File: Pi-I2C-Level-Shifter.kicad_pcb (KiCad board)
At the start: 2 copper layers, 27.9 x 15.2 mm, 9 parts, among them J1 Conn_01x05, J4 Conn_01x05, U1 TXB0102DCT

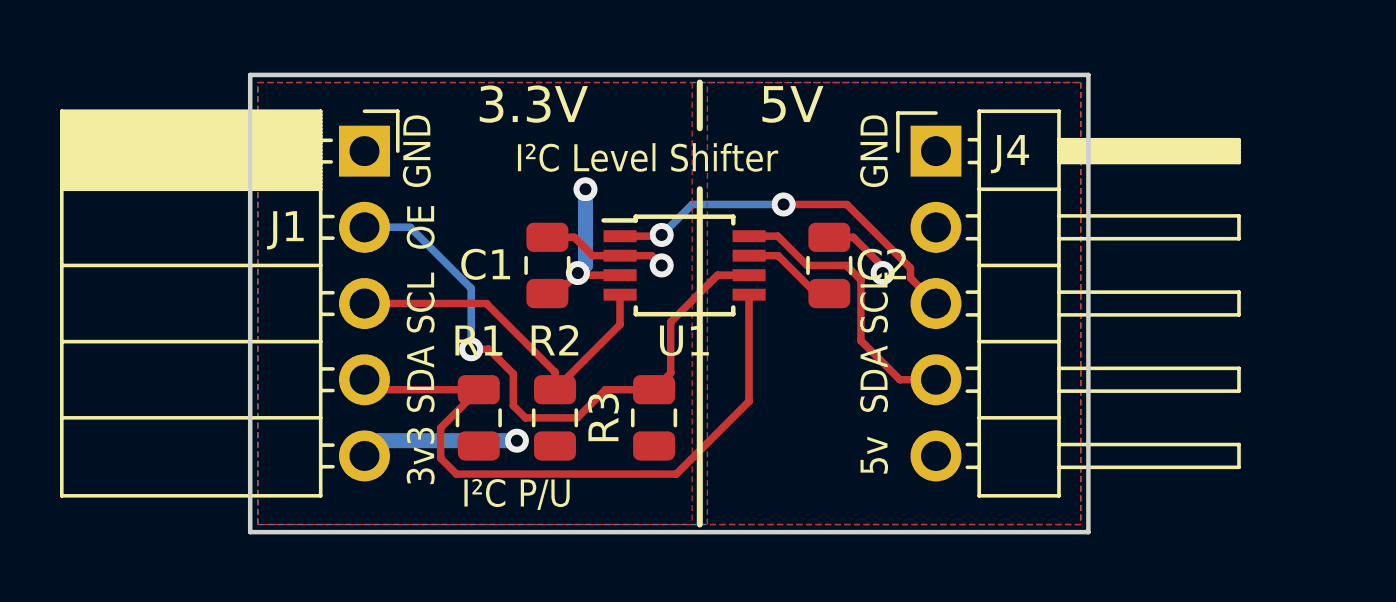
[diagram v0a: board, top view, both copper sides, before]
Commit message: Added 5v GPIO (8 bits)
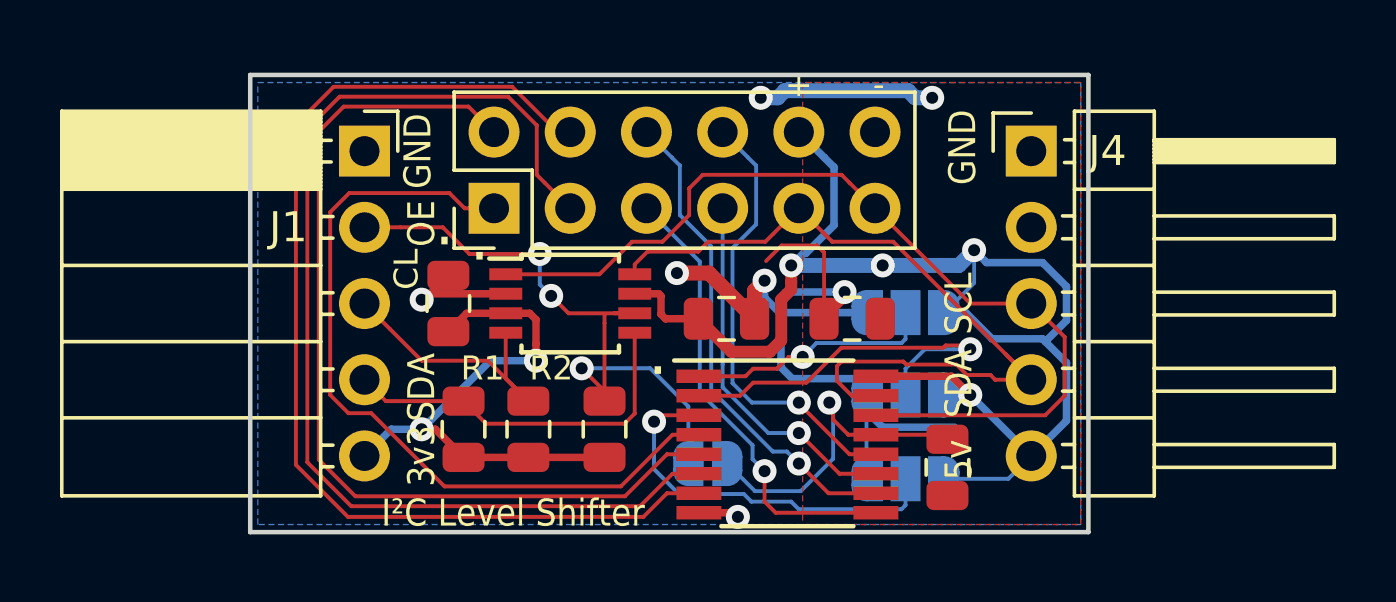
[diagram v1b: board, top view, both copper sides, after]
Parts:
- added C3: 0.1uF, Capacitor_SMD:C_0805_2012Metric, F.Cu at (199.1, 86.9)
- added J2: Conn_02x06_Odd_Even, Connector_PinHeader_2.54mm:PinHeader_2x06_P2.54mm_Vertical, F.Cu at (187.2, 83.2)
- added JP1: SolderJumper_2_Open, Jumper:SolderJumper-2_P1.3mm_Open_RoundedPad1.0x1.5mm, B.Cu at (194.3, 91.7)
- added JP2: SolderJumper_3_Open, Jumper:SolderJumper-3_P1.3mm_Open_RoundedPad1.0x1.5mm, B.Cu at (200.9, 92.2)
- added JP3: SolderJumper_3_Open, Jumper:SolderJumper-3_P1.3mm_Open_RoundedPad1.0x1.5mm, B.Cu at (200.9, 89.4)
- added JP4: SolderJumper_3_Open, Jumper:SolderJumper-3_P1.3mm_Open_RoundedPad1.0x1.5mm, B.Cu at (200.9, 86.7)
- added R4: 10k, Resistor_SMD:R_0805_2012Metric, F.Cu at (202.3, 91.8)
- added U2: TCA9534, Package_SO:TSSOP-16_4.4x5mm_P0.65mm, F.Cu at (197.0, 91.1)
- moved REF** 8.80 mm to (187.8, 87.9)
- moved U1 4.02 mm to (189.7, 86.4)
- moved C2 3.86 mm to (194.9, 86.9), turned to 0 degrees
- moved C1 3.54 mm to (185.7, 86.4)
- moved J4 3.17 mm to (205.1, 81.3)
- moved R3 1.69 mm to (190.9, 90.6)
- moved R2 0.97 mm to (188.3, 90.6)
- moved R1 0.64 mm to (186.2, 90.6)
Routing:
- net Vccb: track 3.20 -> 48.0 mm, vias 0 -> 4
- net P2: track 0.00 -> 36.9 mm
- net P3: track 0.00 -> 36.1 mm
- net Earth: track 6.59 -> 41.3 mm, vias 2 -> 7
- net P1: track 0.00 -> 31.2 mm
- net P0: track 0.00 -> 26.3 mm
- net SCLb: track 12.5 -> 31.3 mm, vias 2 -> 0
- net SDAb: track 9.40 -> 27.4 mm
- net P5: track 0.00 -> 16.4 mm, vias 0 -> 1
- net P4: track 0.00 -> 15.3 mm, vias 0 -> 1
- net P7: track 0.00 -> 14.9 mm, vias 0 -> 1
- net A2: track 0.00 -> 13.5 mm, vias 0 -> 1
- net A1: track 0.00 -> 12.8 mm, vias 0 -> 1
- net P6: track 0.00 -> 12.3 mm, vias 0 -> 1
- net Net-(JP1-Pad2): track 0.00 -> 10.9 mm, vias 0 -> 1
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- removed copper zone on F.Cu, net Vcca
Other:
- rule trace_min: 0.2 -> 0.127
- board text added: "+"
- board text added: "-"
- board text added: "----"
- board text added: "."
- board text added: "0"
- board text added: "1"
- board text added: "2"
- board text added: "A0"
- board text added: "A1"
- board text added: "A2"
- board text added: "C"
- board text added: "CL"
- board text added: "D"
- board text added: "GPIO (5v)"
- board text added: "INT"
- board text removed: "I²C P/U"

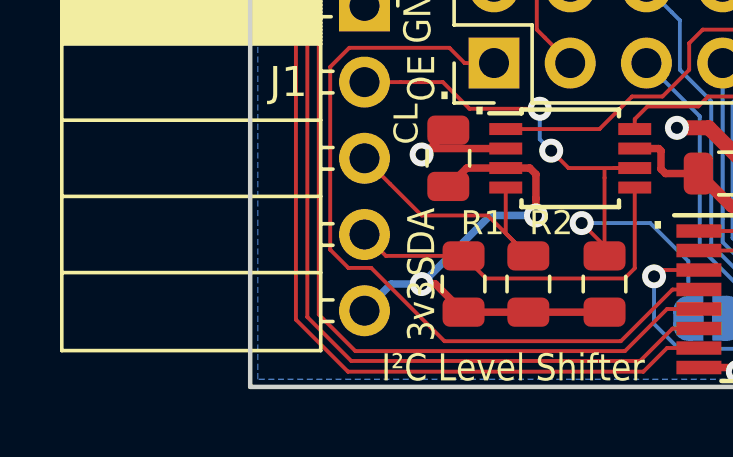
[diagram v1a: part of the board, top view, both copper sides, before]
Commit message: Added fiducial
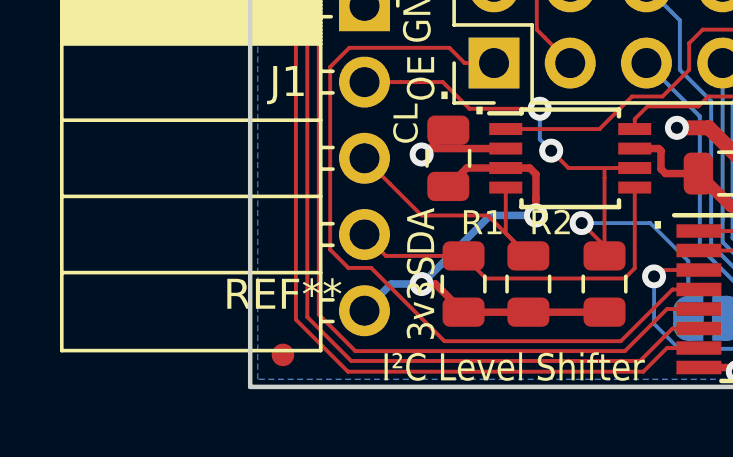
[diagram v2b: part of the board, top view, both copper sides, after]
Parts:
- added REF**: Fiducial_0.75mm_Dia_1.5mm_Outer, Fiducial:Fiducial_0.75mm_Dia_1.5mm_Outer, F.Cu at (180.2, 92.9)
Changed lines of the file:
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@@
     (tracks 303)
     (zones 0)
-    (modules 17)
+    (modules 18)
     (nets 22)
   )
@@
       (padsonsilk false)
       (subtractmaskfromsilk false)
-      (outputformat 0)
+      (outputformat 1)
       (mirror false)
       (drillshape 0)
       (scaleselection 1)
-      (outputdirectory "pdf/"))
+      (outputdirectory "gerber/"))
   )
   (net 0 "")
@@
       (xy -1.971615 -1.454739) (xy -1.908759 -1.469184)) (layer B.SilkS) (width 0.01))
   )
+  (module Fiducial:Fiducial_0.75mm_Dia_1.5mm_Outer (layer F.Cu)
+    (at 180.1622 92.9132)
+    (descr "Circular Fiducial, 0.75mm bare copper top; 1.5mm keepout (Level B)")
+    (tags marker)
+    (attr virtual)
+    (fp_text reference REF** (at 0 -2) (layer F.SilkS)
+      (effects (font (size 1 1) (thickness 0.15)))
+    )
+    (fp_text value Fiducial_0.75mm_Dia_1.5mm_Outer (at 0 2) (layer F.Fab)
+      (effects (font (size 1 1) (thickness 0.15)))
+    )
+    (fp_circle (center 0 0) (end 1 0) (layer F.CrtYd) (width 0.05))
+    (fp_text user %R (at 0 0) (layer F.Fab)
+      (effects (font (size 0.3 0.3) (thickness 0.05)))
+    )
+    (fp_circle (center 0 0) (end 0.75 0) (layer F.Fab) (width 0.1))
+    (pad ~ smd circle (at 0 0) (size 0.75 0.75) (layers F.Cu F.Mask)
+      (solder_mask_margin 0.375) (clearance 0.375))
+  )
   (gr_text . (at 186.7154 84.201) (layer F.SilkS)
     (effects (font (size 1.5 1.5) (thickness 0.3)))
@@
     (effects (font (size 1.1 1.1) (thickness 0.15)) (justify mirror))
   )
-  (gr_poly (pts (xy 204.724 91.0717) (xy 204.8256 91.0844) (xy 204.9145 91.1225) (xy 204.978 91.1733) (xy 205.0415 91.2368) (xy 205.0796 91.3384) (xy 205.0923 91.4273) (xy 205.0923 91.5035) (xy 205.0669 91.5924) (xy 205.0288 91.6559) (xy 204.9399 91.7448) (xy 204.8764 91.7829) (xy 204.7875 91.8083) (xy 204.6605 91.8083) (xy 204.5716 91.7829) (xy 204.5081 91.7448) (xy 204.4192 91.6559) (xy 204.3684 91.5543) (xy 204.3557 91.5035) (xy 204.3557 91.3765) (xy 204.3938 91.2622) (xy 204.5081 91.1352) (xy 204.5716 91.0971) (xy 204.6605 91.0717) (xy 204.6859 91.0717)) (layer F.Paste) (width 0.15))
+  (gr_poly (pts (xy 180.1622 92.5322) (xy 180.2638 92.5449) (xy 180.3527 92.583) (xy 180.4162 92.6338) (xy 180.4797 92.6973) (xy 180.5178 92.7989) (xy 180.5305 92.8878) (xy 180.5305 92.964) (xy 180.5051 93.0529) (xy 180.467 93.1164) (xy 180.3781 93.2053) (xy 180.3146 93.2434) (xy 180.2257 93.2688) (xy 180.0987 93.2688) (xy 180.0098 93.2434) (xy 179.9463 93.2053) (xy 179.8574 93.1164) (xy 179.8066 93.0148) (xy 179.7939 92.964) (xy 179.7939 92.837) (xy 179.832 92.7227) (xy 179.9463 92.5957) (xy 180.0098 92.5576) (xy 180.0987 92.5322) (xy 180.1241 92.5322)) (layer F.Paste) (width 0.15))
   (gr_text VINTLABS.COM (at 180.467 86.36 270) (layer B.SilkS)
     (effects (font (size 1.3 1.3) (thickness 0.3)) (justify mirror))
